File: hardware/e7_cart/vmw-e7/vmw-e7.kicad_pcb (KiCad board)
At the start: 2 copper layers, 70.6 x 95.2 mm, 8 parts, among them J1 Conn_01x02_Pin, J2 Conn_01x02_Pin, U1 E7, U2 ROM, U3 ROM, U4 SRAM, U5 2600Cartridge

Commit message: e7: clip off some unneeded parts of the board
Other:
- board size 70.6 x 95.2 mm -> 70.6 x 88.6 mm
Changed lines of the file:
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@@
 			(at 13.97 0 180)
 			(size 1.524 4.572)
-			(layers "F.Mask" "F.Cu")
+			(layers "F.Cu" "F.Mask")
 			(net 7 "D3")
 			(pinfunction "D3")
@@
 	)
 	(gr_line
+		(start 162.3314 40.64)
+		(end 91.7448 40.64)
+		(stroke
+			(width 0.05)
+			(type default)
+		)
+		(layer "Edge.Cuts")
+	)
+	(gr_line
 		(start 143.256 129.286)
 		(end 143.256 116.586)
@@
 	(gr_line
 		(start 91.694 97.536)
-		(end 91.694 34.036)
+		(end 91.7448 40.64)
 		(stroke
 			(width 0.05)
@@
 	(gr_line
 		(start 162.306 97.536)
-		(end 162.306 34.036)
+		(end 162.3314 40.64)
 		(stroke
 			(width 0.05)
@@
 		(stroke
 			(width 0.05)
-			(type default)
-		)
-		(layer "Edge.Cuts")
-	)
-	(gr_line
-		(start 162.306 34.036)
-		(end 91.694 34.036)
-		(stroke
-			(width 0.05)

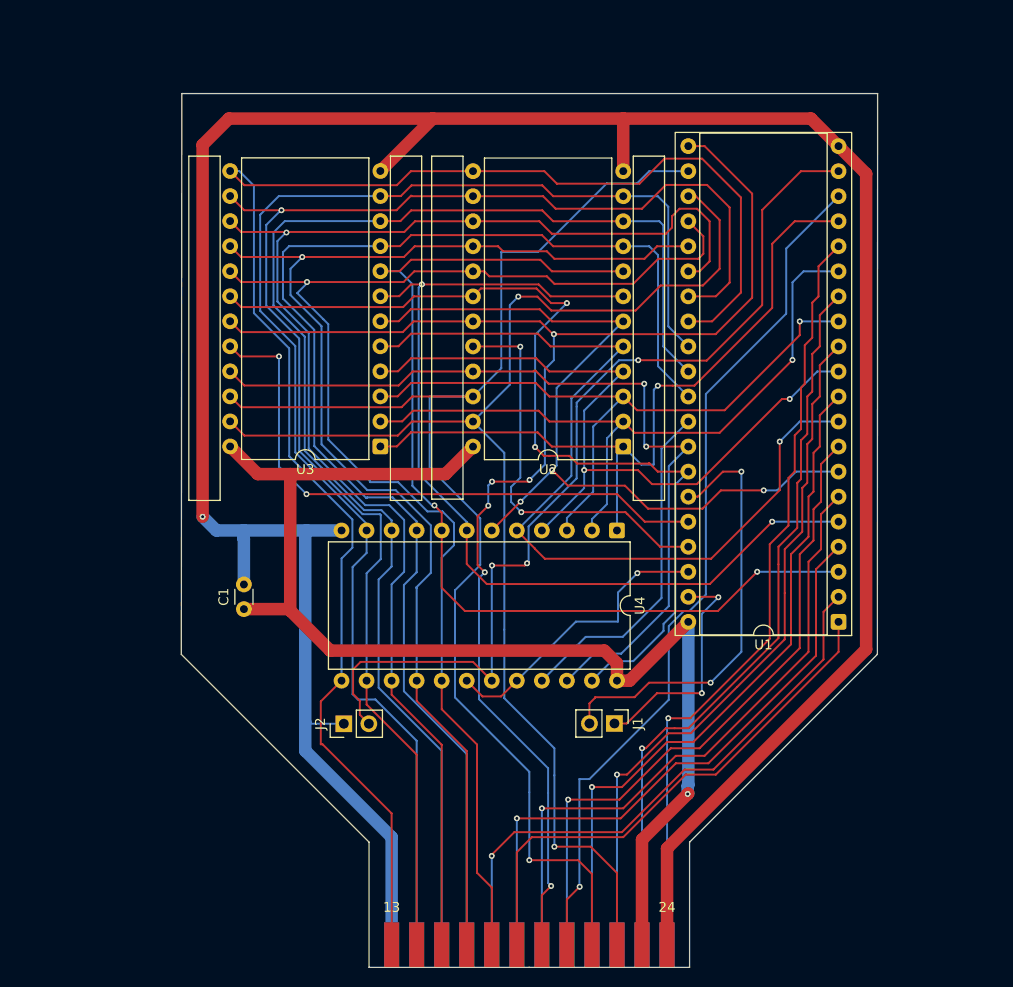
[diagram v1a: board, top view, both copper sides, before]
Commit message: e7: add another filter cap, give some more clearance to DIP pins
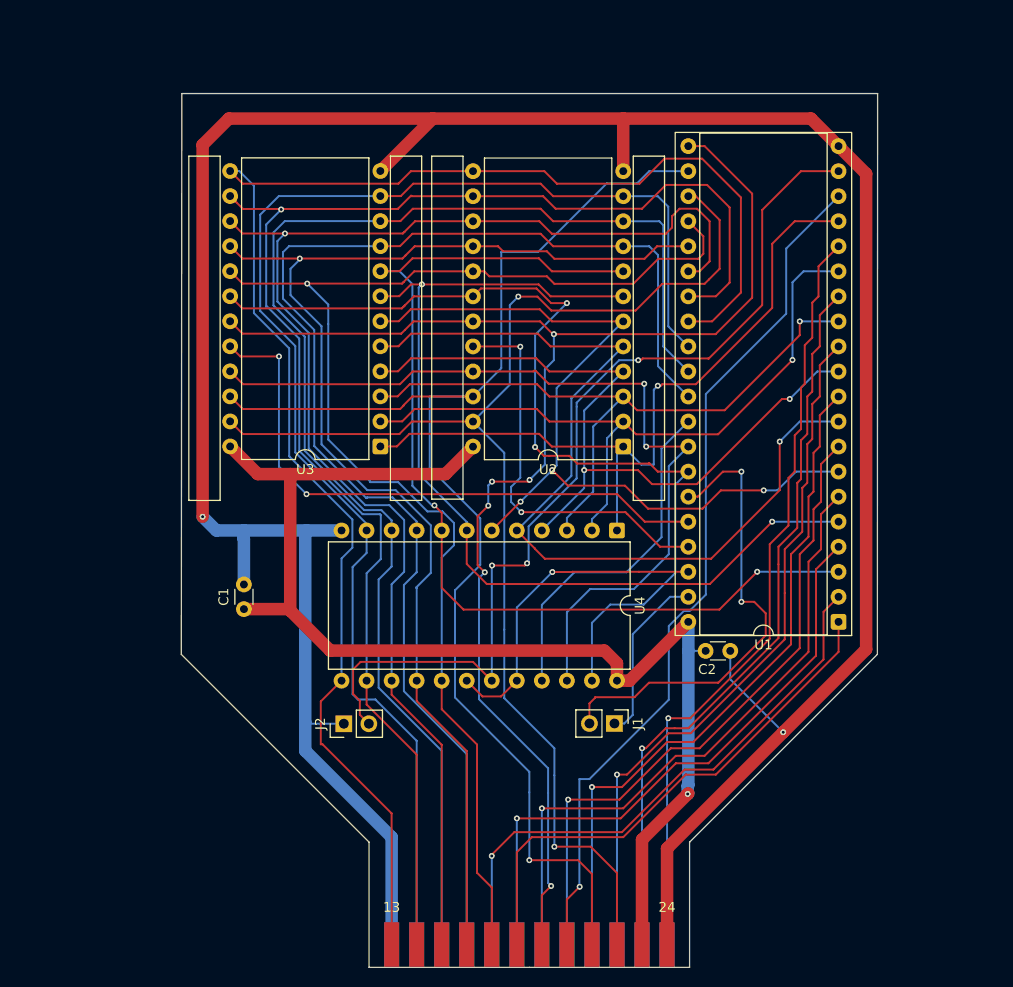
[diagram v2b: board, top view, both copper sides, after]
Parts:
- added C2: C_US, Capacitor_THT:C_Disc_D3.0mm_W1.6mm_P2.50mm, F.Cu at (144.9, 97.2)
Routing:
- net GNDREF: track 277.8 -> 288.3 mm, vias 1 -> 2
- net 128k: track 23.7 -> 17.6 mm, vias 2 -> 0
- net A13: track 44.4 -> 47.7 mm
- net ~{OE}: track 30.1 -> 32.7 mm
- net VCC: track 127.3 -> 129.1 mm
- net A11ROM_A8RAM: track 95.1 -> 96.1 mm
- net D7: track 134.1 -> 133.2 mm
- net ~{WE}: track 34.6 -> 35.5 mm
- net A12ROM_A9RAM: track 85.1 -> 86.0 mm

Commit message: e7: add silkscreen
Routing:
- net A11: track 88.3 -> 87.7 mm
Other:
- board text added: "128K"
- board text added: "1K/2K SRAM"
- board text added: "A Hardware Production (2026)"
- board text added: "A13?"
- board text added: "GND"
- board text added: "ROM1 (8K)"
- board text added: "ROM2 (4K/8K)"
- board text added: "THIS SIDE TOWARD ENEMY (THE ENEMY IS YOU)"
- board text added: "THIS SIDE TOWARD TV"
- board text added: "VCS E7/EPROM Cartridge -- Mark 1"
- board text added: "{dblquote}Big Game{dblquote} E7"
- board text added: "{dblquote}W1{dblquote} (A10)"

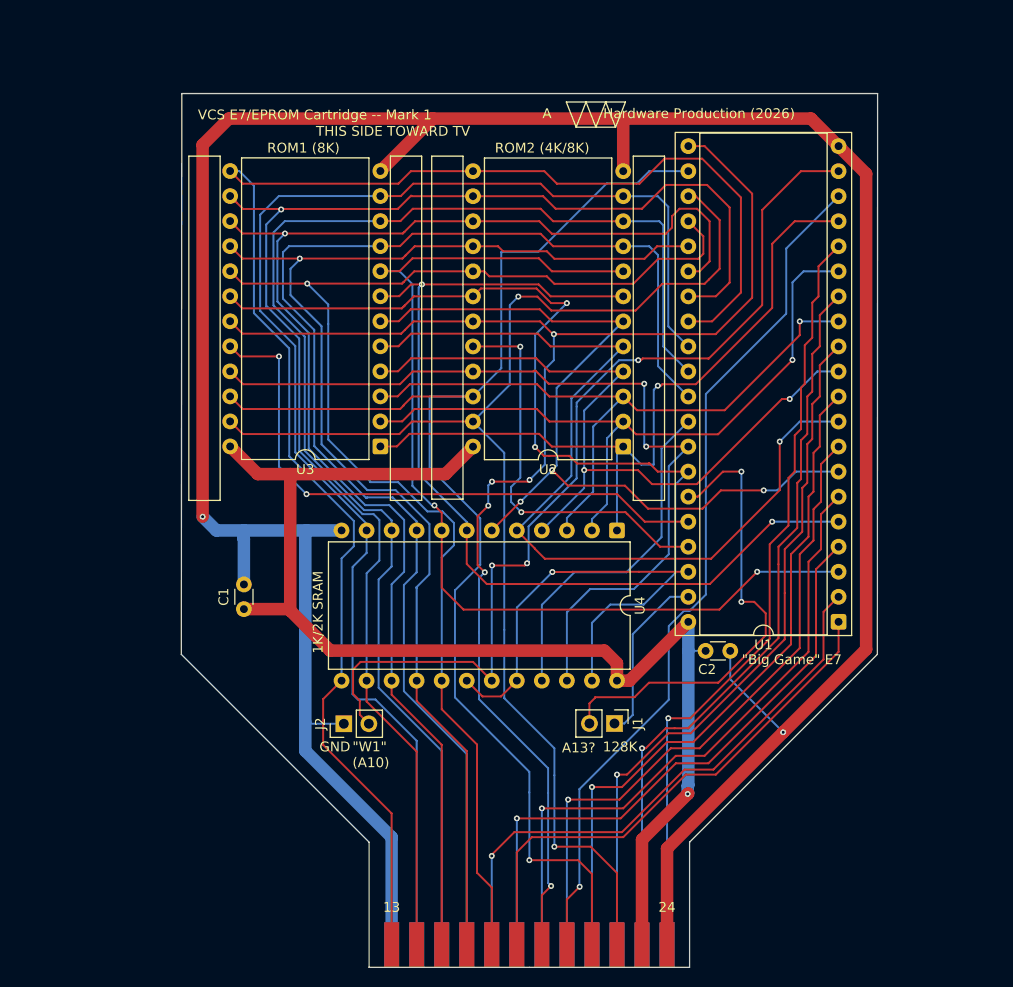
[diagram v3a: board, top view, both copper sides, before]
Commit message: e7: do a ground pour
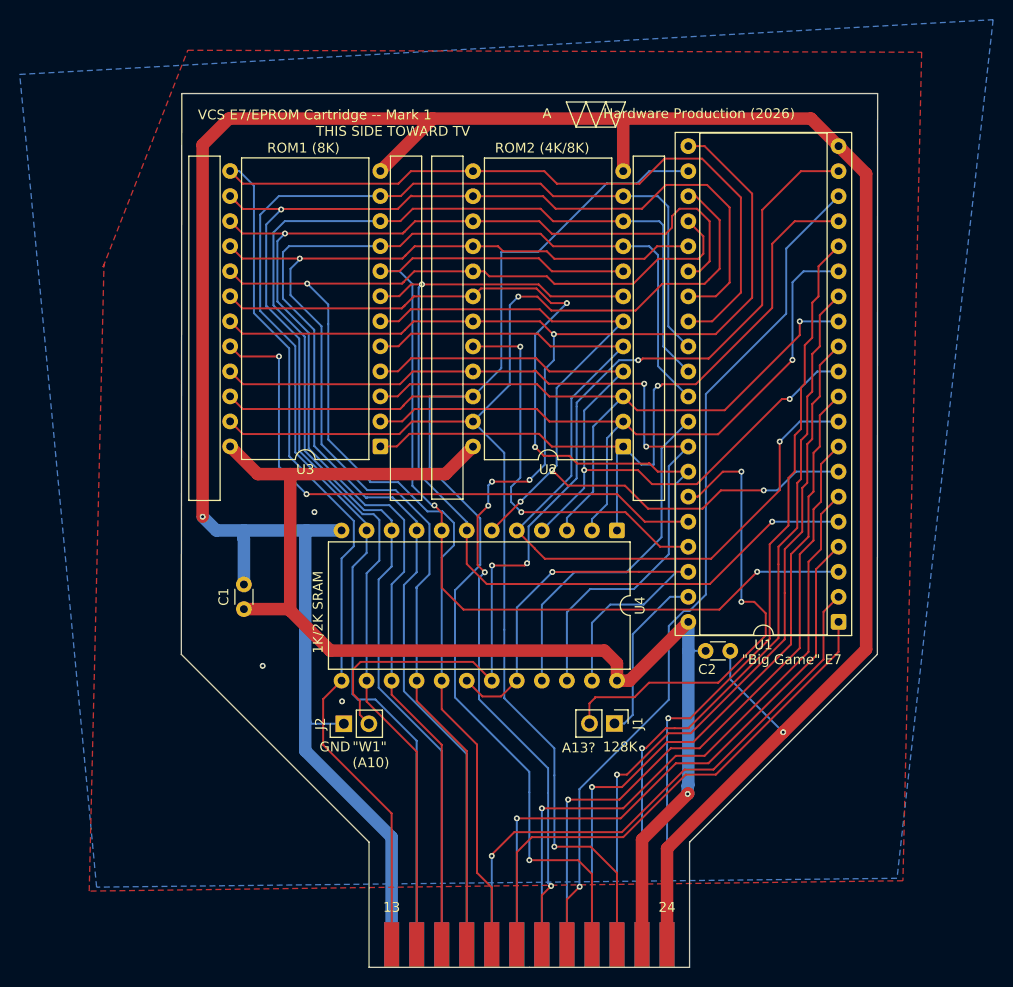
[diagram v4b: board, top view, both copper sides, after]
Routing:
- net GNDREF: vias 2 -> 5
- added copper zone on B.Cu, net GNDREF
- added copper zone on F.Cu, net GNDREF
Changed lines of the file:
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@@
 	)
 	(via
+		(at 108 102.3)
+		(size 0.6)
+		(drill 0.3)
+		(layers "F.Cu" "B.Cu")
+		(free yes)
+		(net 2)
+	)
+	(via
+		(at 105.2 83.1)
+		(size 0.6)
+		(drill 0.3)
+		(layers "F.Cu" "B.Cu")
+		(free yes)
+		(net 2)
+	)
+	(via
+		(at 99.95 98.7)
+		(size 0.6)
+		(drill 0.3)
+		(layers "F.Cu" "B.Cu")
+		(free yes)
+		(net 2)
+	)
+	(via
 		(at 152.7556 105.4354)
 		(size 0.6)
@@
 		(net 40)
 	)
+	(zone
+		(net 2)
+		(net_name "GNDREF")
+		(layer "F.Cu")
+		(hatch edge 0.5)
+		(connect_pads
+			(clearance 0.5)
+		)
+		(min_thickness 0.25)
+		(filled_areas_thickness no)
+		(fill yes
+			(thermal_gap 0.5)
+			(thermal_bridge_width 0.5)
+		)
+		(polygon
+			(pts
+				(xy 83.75 58.25) (xy 92.35 36.25) (xy 166.8 36.45) (xy 164.9 120.5) (xy 82.35 121.55) (xy 83.85 58)
+			)
+		)
+	)
+	(zone
+		(net 2)
+		(net_name "GNDREF")
+		(layer "B.Cu")
+		(hatch edge 0.5)
+		(priority 1)
+		(connect_pads
+			(clearance 0.5)
+		)
+		(min_thickness 0.25)
+		(filled_areas_thickness no)
+		(fill yes
+			(thermal_gap 0.5)
+			(thermal_bridge_width 0.5)
+		)
+		(polygon
+			(pts
+				(xy 75.3 38.7) (xy 174.05 33.15) (xy 164.3 120.25) (xy 83.1 121.15)
+			)
+		)
+	)
 	(group ""
